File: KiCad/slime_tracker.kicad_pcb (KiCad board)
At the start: 2 copper layers, 80.2 x 32 mm, 50 parts, among them J1 batt, J2 Extension, J3 USB_C_Receptacle_PowerOnly_6P, SW1 SW_DPDT_x2, U1 TP4056, U3 TPS7A0333PDBVR, U4 ESP32 SUPER MINI C3, U5 TPS61090

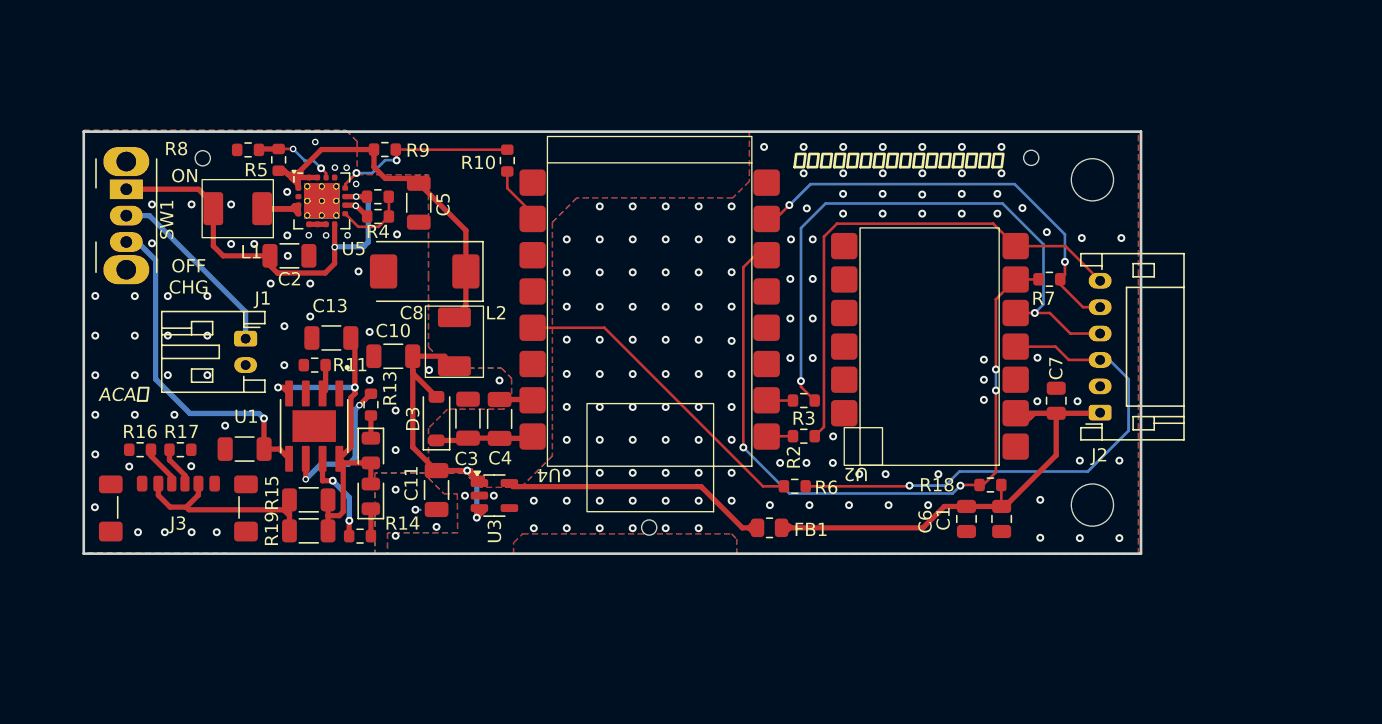
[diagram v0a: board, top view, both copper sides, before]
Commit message: REV0.3
REV 0.3

TVS, EN/CE Based control, SPI I2C selectable Footprint, ESP32 Footprint changed,  etc
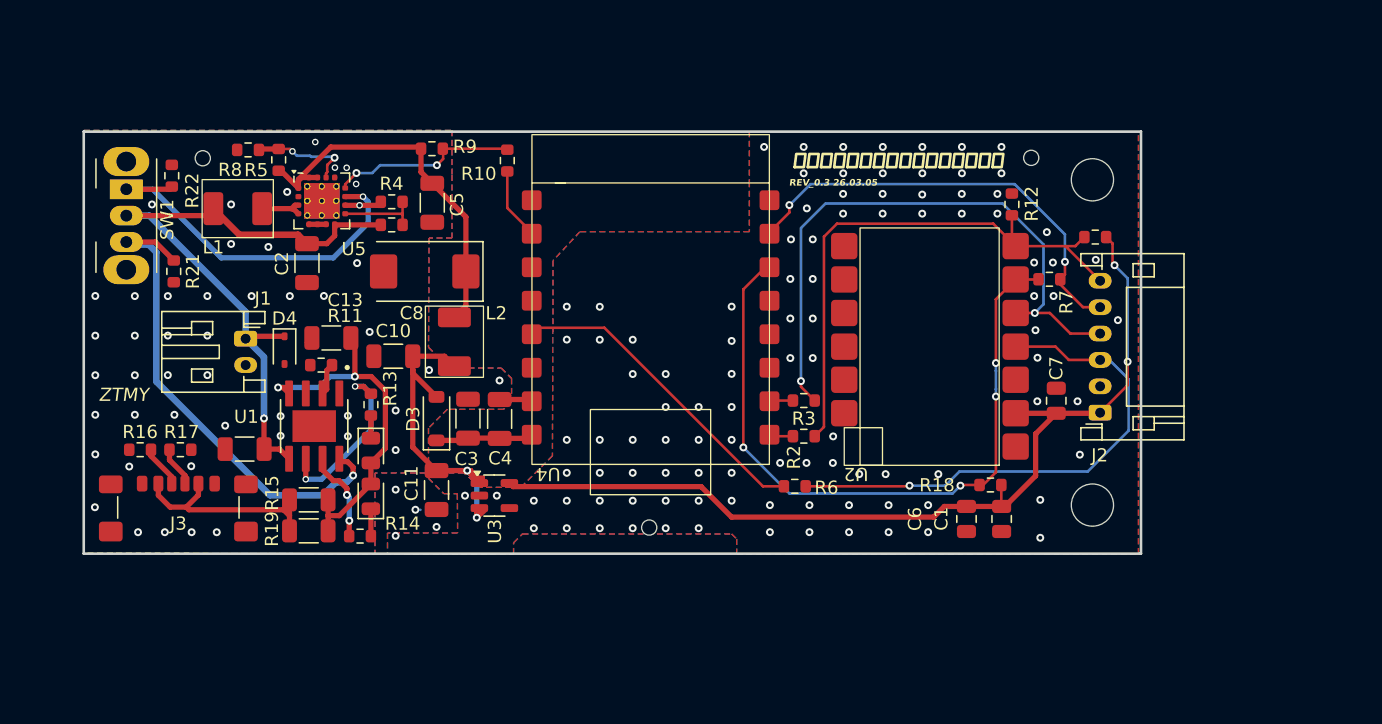
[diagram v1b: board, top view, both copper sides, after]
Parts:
- removed FB1: FerriteBead, Resistor_SMD:R_0805_2012Metric
- added D4: D_TVS, Diode_SMD:D_SOD-323, F.Cu at (78.8, 61.0)
- added R12: 0Ω, Resistor_SMD:R_0603_1608Metric, F.Cu at (133.9, 50.0)
- added R20: 0Ω, Resistor_SMD:R_0603_1608Metric, F.Cu at (140.3, 52.4)
- added R21: 100kΩ, Resistor_SMD:R_0603_1608Metric, F.Cu at (70.4, 55.0)
- added R22: 100kΩ, Resistor_SMD:R_0603_1608Metric, F.Cu at (70.2, 47.8)
- C1: value 1uF -> 10nF
- C6: value 10uF -> 100nF
- C7: value 0.1uF -> 1nF
- moved R9 3.57 mm to (90.0, 45.7)
- moved R1 2.38 mm to (86.9, 51.5)
- moved R4 1.52 mm to (86.9, 49.8)
- moved C2 1.44 mm to (80.5, 54.4), turned to 90 degrees
- moved C5 1.02 mm to (90.0, 49.8)
- moved U4 0.60 mm to (106.6, 73.9)
- moved R11 0.49 mm to (81.6, 62.1)
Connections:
- C12 pad 1: BAT-_TO_CHG -> BAT+
- C2 pad 2: BAT-_TO_BOOST -> BAT+
- L1 pad 1: BAT-_TO_BOOST -> BAT+
- R1 pad 1: BAT-_TO_BOOST -> BAT+
- U1 pad 5: BAT-_TO_CHG -> BAT+
- U1 pad 8: Net-(D1-A) -> BAT-_TO_CHG
- U3 pad 5: Net-(U3-OUT) -> 3v3
- U5 pad 8: BAT-_TO_BOOST -> BAT+
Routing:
- net 3v3: track 34.4 -> 70.6 mm, vias 0 -> 2
- net BAT+: track 14.1 -> 50.1 mm, vias 0 -> 1
- net Net-(U3-OUT): track 20.2 -> 0.00 mm
- net BAT-_TO_CHG: track 25.8 -> 37.8 mm
- net Net-(L1-Pad2): track 9.20 -> 3.54 mm
- net MISO: track 38.6 -> 42.7 mm
- net BAT-_TO_BOOST: track 32.5 -> 28.7 mm, vias 2 -> 1
- net Net-(U1-!STDBY): track 11.3 -> 13.7 mm
- net Net-(U5-FB): track 6.14 -> 7.71 mm
- net Net-(D1-A): track 28.5 -> 27.1 mm
- net 5V_B_FIL: track 31.1 -> 29.7 mm
- net Net-(U2-CS): track 54.1 -> 53.0 mm
- net BAT_LOW_SIG: track 4.39 -> 5.39 mm
- net BAT-: track 6.80 -> 7.51 mm, vias 186 -> 154
- net Net-(U5-LBI): track 5.55 -> 6.12 mm
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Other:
- board text added: "REV_0.3 26.03.05"
- board text added: "ZTMY"
- board text removed: "ACAね"
- board text removed: "OFF CHG"
- board text removed: "ON"

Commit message: REV3 TD
TeadDrop
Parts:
- C8: footprint Capacitor_Tantalum_SMD:CP_EIA-7343-20_Kemet-V -> Capacitor_Tantalum_SMD:CP_EIA-7343-31_Kemet-D
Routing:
- net Net-(U5-FB): track 7.71 -> 8.37 mm
- net BAT-: vias 154 -> 152

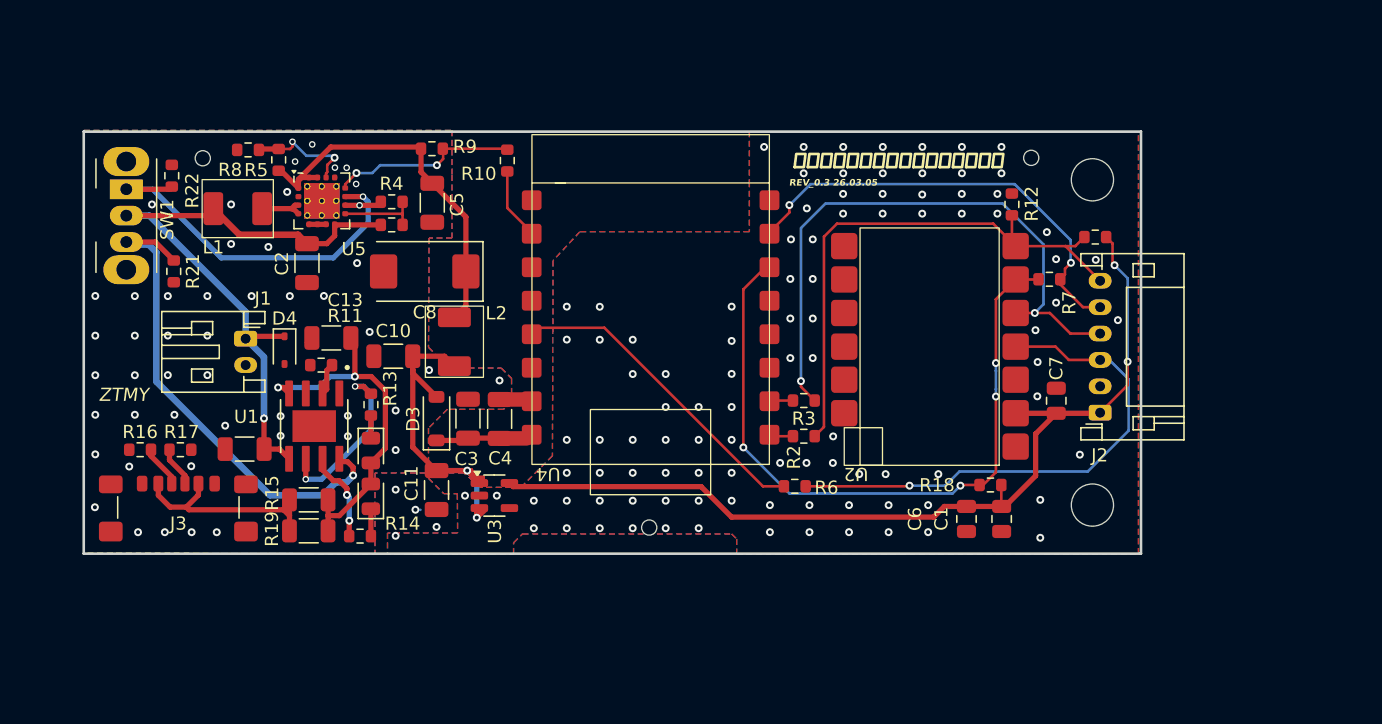
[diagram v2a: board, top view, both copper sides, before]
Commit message: Rev 03 more TVS
more TVS at extend port line
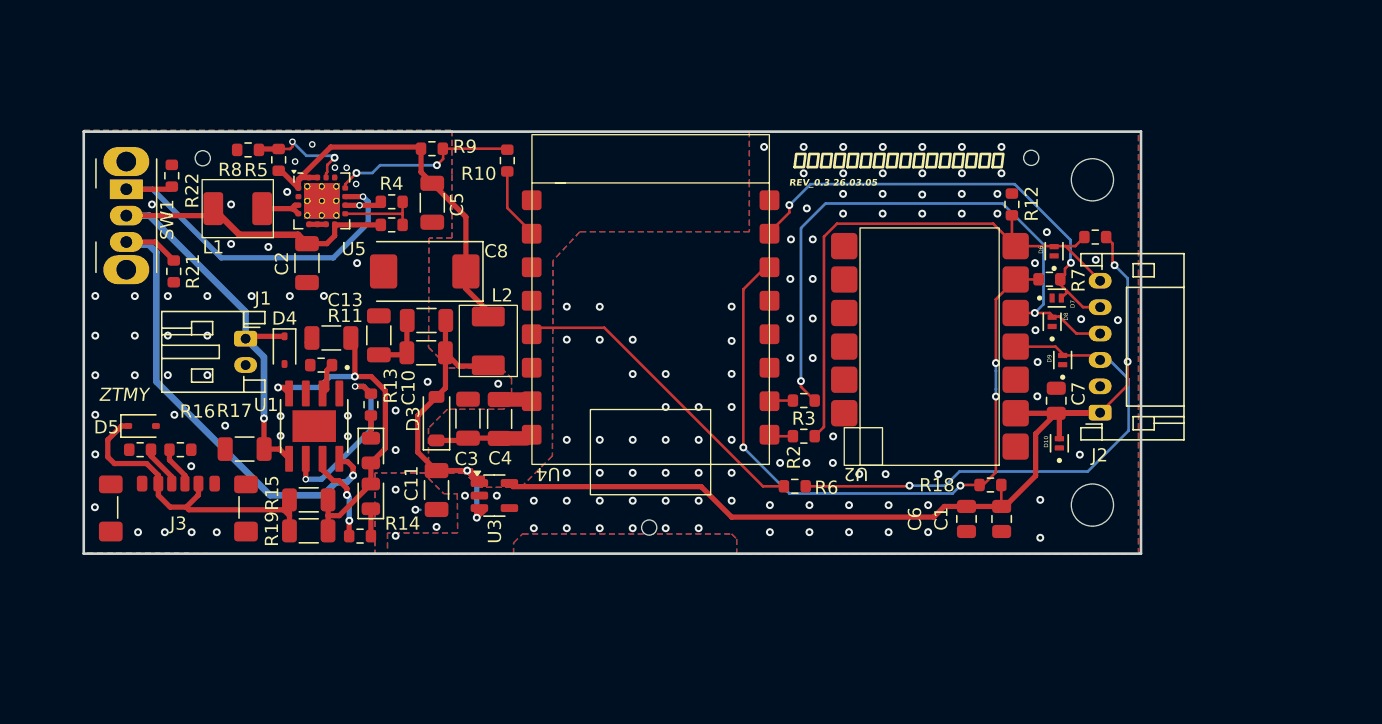
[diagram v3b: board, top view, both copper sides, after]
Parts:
- added D10: D_TVS, slime:DFN1006-2, F.Cu at (137.6, 68.1)
- added D5: D_TVS, Diode_SMD:D_SOD-323, F.Cu at (68.0, 66.8)
- added D6: D_TVS, slime:DFN1006-2, F.Cu at (137.2, 53.5)
- added D7: D_TVS, slime:DFN1006-2, F.Cu at (137.3, 57.0)
- added D8: D_TVS, slime:DFN1006-2, F.Cu at (137.0, 58.9)
- added D9: D_TVS, slime:DFN1006-2, F.Cu at (137.8, 61.8)
- added R23: 1Ω, Resistor_SMD:R_1206_3216Metric, F.Cu at (89.6, 58.8)
- added R24: 1Ω, Resistor_SMD:R_1206_3216Metric, F.Cu at (89.5, 61.2)
- moved L2 2.57 mm to (94.2, 60.3)
- moved C10 1.93 mm to (86.0, 59.9), turned to -90 degrees
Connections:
- C10 pad 2: 5V -> Net-(C10-Pad2)
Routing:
- net C-TYPE+: track 16.0 -> 24.3 mm
- net 3v3: track 70.6 -> 75.6 mm
- net Net-(C10-Pad2): track 0.00 -> 4.65 mm
- net 5V: track 25.1 -> 26.0 mm
- net CS2: track 33.9 -> 34.6 mm
- net BAT-: vias 152 -> 149

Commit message: REV03 3/11
few PCB layout changed
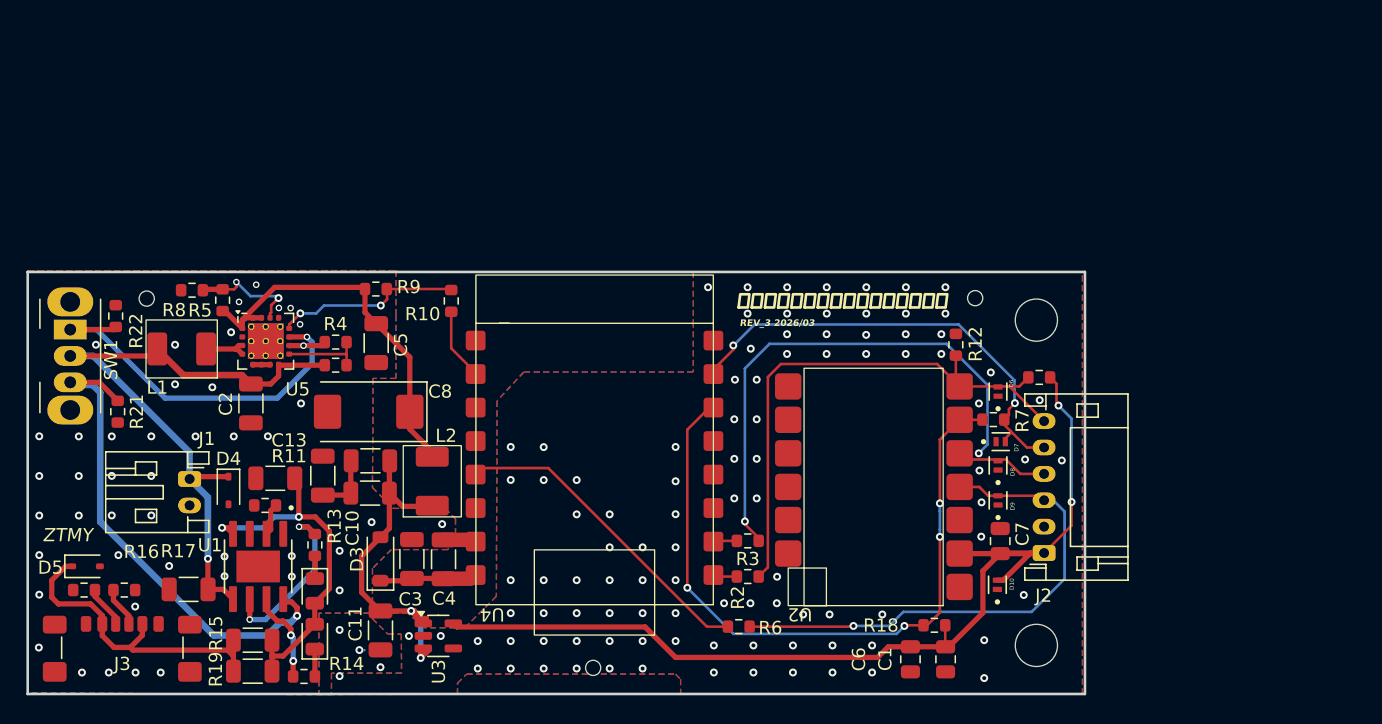
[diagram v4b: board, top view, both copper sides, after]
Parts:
- moved D9 11.7 mm to (132.9, 72.4)
- moved D10 11.7 mm to (132.8, 78.8)
- moved D7 11.7 mm to (133.1, 67.9)
- moved D8 11.6 mm to (132.9, 69.7)
- moved C2 11.5 mm to (76.2, 65.0)
- moved R11 11.5 mm to (77.3, 72.8)
- moved R21 11.5 mm to (66.2, 65.7)
- moved R7 11.5 mm to (132.5, 66.3)
- moved SW1 11.5 mm to (62.6, 59.4)
- moved C1 11.5 mm to (128.9, 84.4)
- moved C10 11.5 mm to (81.7, 70.5)
- moved C11 11.5 mm to (86.1, 82.2)
- moved C12 11.5 mm to (71.5, 79.1)
- moved C13 11.5 mm to (78.1, 70.7)
- moved C3 11.5 mm to (88.5, 76.8)
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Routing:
- net 3v3: track 75.6 -> 78.5 mm
- net SCK: track 39.9 -> 39.3 mm
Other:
- board text added: "REV_3 2026/03"
- board text removed: "REV_0.3 26.03.05"

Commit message: rev03 agnd pgnd
agnd pgnd
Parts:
- moved R8 10.2 mm to (82.0, 57.2), turned to 0 degrees
- moved R5 8.03 mm to (82.0, 58.8), turned to 180 degrees
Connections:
- U4 pad 0: unconnected-(U4-GPIO0/A0-Pad0) -> BAT-
- U4 pad 2: unconnected-(U4-GPIO2/A2-Pad2) -> BAT-
- U4 pad 3: unconnected-(U4-GPIO3/A3-Pad3) -> BAT-
- U4 pad 53: unconnected-(U4-3V3-Pad53) -> BAT-
- U4 pad 7: unconnected-(U4-GPIO7/SS-Pad7) -> BAT-
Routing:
- net BAT-: track 7.51 -> 20.4 mm, vias 149 -> 144
- net 5V_B_FIL: track 30.0 -> 33.1 mm
- net Net-(U5-FB): track 8.37 -> 6.37 mm
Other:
- board text added: "REV_3 2026 /03"
- board text removed: "REV_3 2026/03"

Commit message: LPF Changed
dd
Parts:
- added C16: 22uF, Capacitor_SMD:C_0805_2012Metric, F.Cu at (83.3, 77.0)
- added C9: 4.7uF, Capacitor_SMD:C_0805_2012Metric, F.Cu at (84.5, 70.0)
- C10: value 4.7uF -> 22uF; footprint Capacitor_SMD:C_1206_3216Metric -> Capacitor_SMD:C_0805_2012Metric
- C11, C4, C5: footprint Capacitor_SMD:C_1206_3216Metric -> Capacitor_SMD:C_0603_1608Metric
- C12, C13, C3: footprint Capacitor_SMD:C_1206_3216Metric -> Capacitor_SMD:C_0805_2012Metric
- C6, C7: footprint Capacitor_SMD:C_0805_2012Metric -> Capacitor_SMD:C_0603_1608Metric
- L2: value 2.2uH -> 3uH
- R23, R24: footprint Resistor_SMD:R_1206_3216Metric -> Resistor_SMD:R_0603_1608Metric
- moved R23 6.61 mm to (85.8, 76.0)
- moved C10 3.37 mm to (83.3, 73.5)
- moved R24 2.65 mm to (85.8, 74.4)
- moved D3 2.62 mm to (86.2, 79.5), turned to -90 degrees
- moved L2 1.61 mm to (88.5, 70.5), turned to 0 degrees
- moved C11 1.36 mm to (86.6, 83.5)
- moved C3 0.94 mm to (89.4, 76.8)
- moved C5 0.82 mm to (85.7, 61.3), turned to 0 degrees
- moved R13 0.52 mm to (80.6, 75.9)
- moved C12 0.49 mm to (72.0, 79.1)
- moved C4 0.42 mm to (91.2, 76.6)
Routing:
- net Net-(C10-Pad2): track 4.65 -> 0.10 mm
- net BAT-: track 20.4 -> 17.9 mm, vias 144 -> 153
- net 5V_B_FIL: track 33.1 -> 35.3 mm
- net Net-(D1-A): track 27.1 -> 28.9 mm, vias 2 -> 3
- net 5V: track 26.0 -> 24.8 mm, vias 2 -> 4
- added copper zone on F.Cu, net Net-(C10-Pad2)
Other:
- board text added: "REV_3 2026 03"
- board text removed: "REV_3 2026 /03"
- board text removed: "ZTMY"

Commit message: rev03 almost
com
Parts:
- C5: footprint Capacitor_SMD:C_0603_1608Metric -> Capacitor_SMD:C_0805_2012Metric
- L2: footprint slime:FXL0420 -> slime:FNR5020S3R0NT
- moved C2 3.17 mm to (79.4, 64.9)
- moved C7 2.91 mm to (132.9, 78.4), turned to -90 degrees
- moved D10 2.84 mm to (132.9, 76.0), turned to -90 degrees
- moved L2 2.81 mm to (88.6, 73.3), turned to 180 degrees
- moved D8 1.74 mm to (132.6, 71.5)
- moved D7 1.71 mm to (133.8, 69.5), turned to 90 degrees
- moved D9 1.31 mm to (133.7, 73.4)
- moved R7 1.23 mm to (132.8, 67.5)
- moved C9 0.74 mm to (84.0, 69.5), turned to 0 degrees
- moved C5 0.27 mm to (86.0, 61.3)
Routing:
- net 3v3: track 78.9 -> 71.2 mm
- net MOSI: track 46.6 -> 50.6 mm
- net BAT+: track 50.1 -> 52.9 mm, vias 1 -> 3
- net CS2: track 34.9 -> 37.4 mm
- net 5V: track 24.8 -> 23.7 mm
- net SCK: track 39.3 -> 40.4 mm
- net 5V_B_FIL: track 35.3 -> 36.1 mm
- net Net-(U2-CS): track 53.0 -> 53.7 mm
- net Net-(U5-LBO): track 14.1 -> 14.7 mm
- net BAT-_TO_CHG: track 37.8 -> 37.2 mm
- net BAT-: track 17.9 -> 17.6 mm, vias 153 -> 150
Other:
- board text removed: "REV_3 2026 03"
- board text removed: "ユニちゃんズ＿スライムトラッカー"

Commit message: layout edge cut
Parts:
- moved H5 33.8 mm to (96.2, 37.9)
- moved R22 32.5 mm to (91.8, 38.7)
- moved R21 32.3 mm to (92.6, 47.1), turned to 0 degrees
- moved SW1 31.8 mm to (88.1, 40.5)
- moved H3 28.7 mm to (122.7, 65.0)
- moved L1 28.4 mm to (93.3, 43.3), turned to -90 degrees
- moved J1 27.9 mm to (92.1, 51.9)
- moved D10 27.7 mm to (153.5, 57.4)
- moved D9 27.7 mm to (154.2, 54.8)
- moved R12 27.7 mm to (150.2, 42.0)
- moved R20 27.7 mm to (156.5, 44.5)
- moved C11 27.7 mm to (107.1, 64.9)
- moved C13 27.7 mm to (98.6, 52.1)
- moved C2 27.7 mm to (99.9, 46.3)
- moved C4 27.7 mm to (111.7, 58.0)
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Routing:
- net 5V_B_FIL: track 36.1 -> 29.4 mm
- net BAT+: track 52.9 -> 46.7 mm, vias 3 -> 1
- net BAT-: track 17.6 -> 12.4 mm, vias 150 -> 132
- net BAT-_TO_BOOST: track 28.6 -> 24.7 mm
- net Net-(L1-Pad2): track 3.54 -> 0.00 mm
- net BAT-_TO_CHG: track 37.2 -> 37.7 mm
- added copper zone on F.Cu, net 5V_B_FIL
- added copper zone on F.Cu, net Net-(L1-Pad2)
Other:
- outline, holes or cut-outs redrawn
